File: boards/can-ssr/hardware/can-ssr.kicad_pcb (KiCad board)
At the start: 2 copper layers, 100 x 100 mm, 127 parts, among them J1 CAN IN, J2 CAN OUT, J3 ICSP, J30 MEAN WELL, J4 UART, Q1 IPB110N20N3LF, Q2 IPB110N20N3LF, Q20 2N7002, Q21 2N7002, Q22 2N7002, Q23 2N7002, Q24 2N7002, Q3 IPB110N20N3LF, Q4 IPB110N20N3LF, Q5 MMBT2907A, SW1 ADDR, U1 R-78E5.0-1.0, U10 VOM1271T, U11 VOM1271T, U12 ACS770ECB-100U-PFF-T, U2 MCP2562FD-E/P, U20 LM393B, U3 PIC18F47Q84-I/PT, U30 UCC12050DVE, U31 ISO1640DWR, U32 MCP3426A0-E/SN, U33 MCP4725A0T-E/CH, U34 MCP4725A0T-E/CH, U35 TLP222A, U36 MCP3426A1-E/SN, U40 MAX7219CWG+, U41 CC56-12SRWA, Y1 16MHz

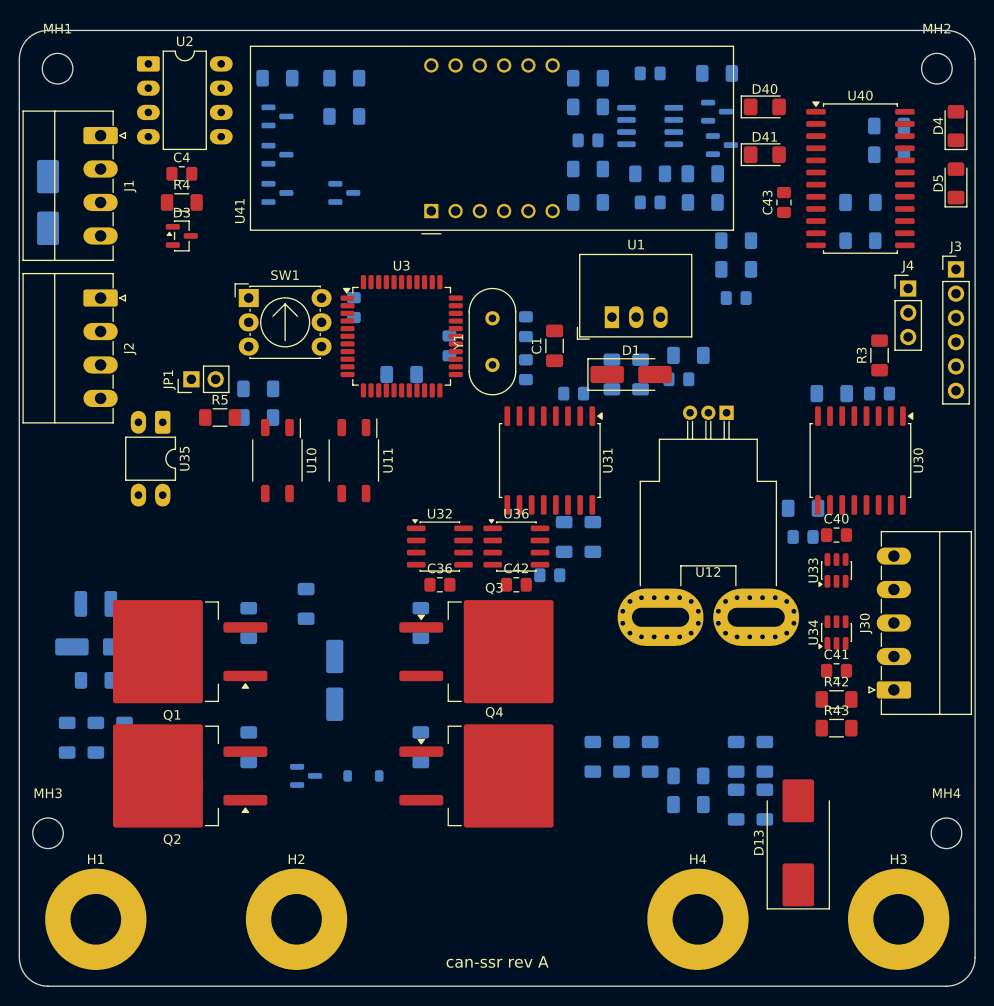
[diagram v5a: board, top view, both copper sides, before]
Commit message: can-ssr: power copper, barrier keep-out, busbar strips, HV rules
- Top pours: VIN, SRC, VOUT_SW, VOUT; RET at the S-/L- bolts; GND_LOAD
  pour across the load half on the bottom; logic GND both sides
- 6 mm barrier keep-out (y 42-48) on both layers
- Solder-mask openings for the bars: VIN, VOUT_SW, VOUT (1/2 in), source
  node (1/4 in), return bar (bottom); 12-via rings at S- and L-
- Net classes HV and GD plus 1.5 mm clearance rules in can-ssr.kicad_dru
- L+ moved to x 86 for a straight VOUT bar; D13, DACs and dividers to
  the bottom; dividers chained end to end; MH3 clear of the S+ bar

Co-Authored-By: Claude Opus 5.5 <noreply@anthropic.com>
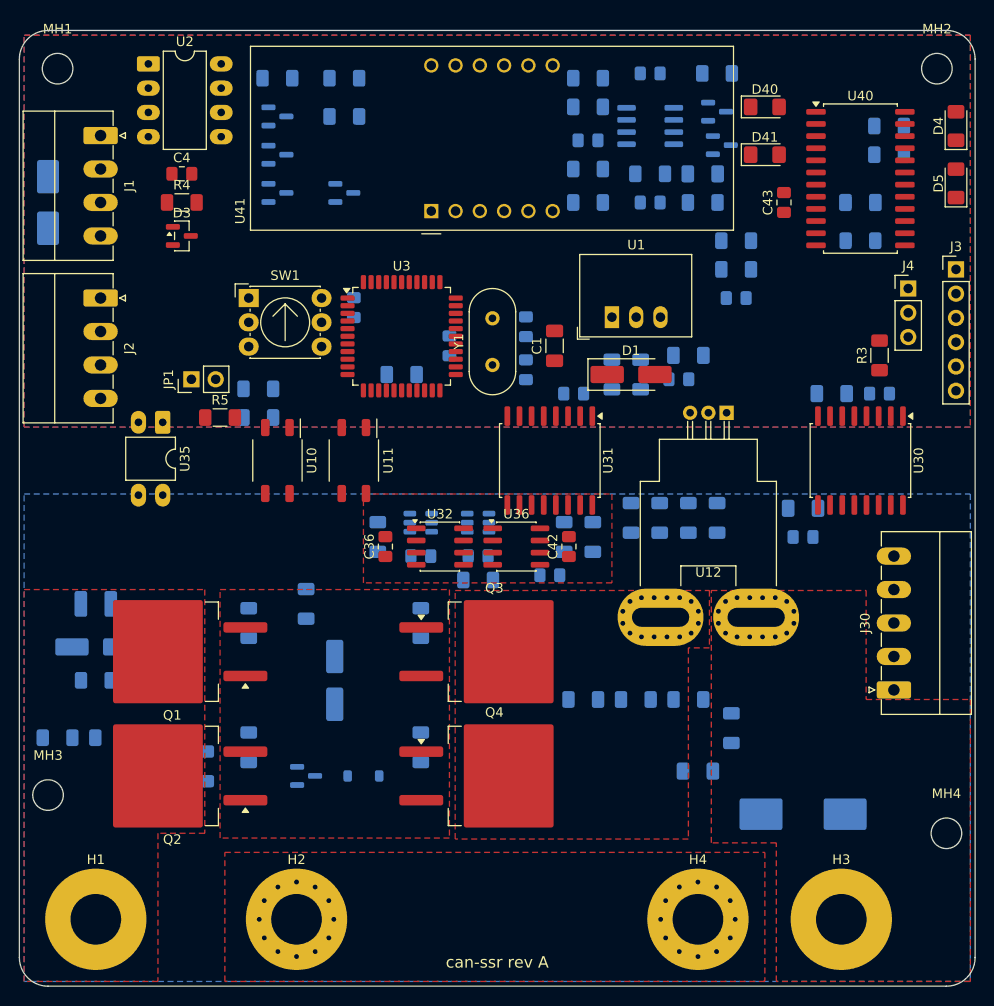
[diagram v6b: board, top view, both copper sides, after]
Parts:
- C40, C41, D13, R42, R43, U33, U34: moved to B.Cu
- moved R42 50.9 mm to (137.5, 153.0), turned to 90 degrees
- moved U33 43.8 mm to (142.0, 151.5), turned to 0 degrees
- moved C40 43.6 mm to (142.0, 155.0)
- moved R43 40.6 mm to (148.0, 157.5)
- moved C41 39.4 mm to (148.0, 155.0)
- moved U34 39.2 mm to (148.0, 151.5), turned to 0 degrees
- moved R45 31.0 mm to (167.0, 151.0)
- moved R47 30.4 mm to (173.0, 151.0)
- moved R44 27.3 mm to (164.0, 151.0)
- moved R46 26.2 mm to (170.0, 151.0)
- moved R40 7.21 mm to (170.0, 170.0), turned to 0 degrees
- moved C36 6.96 mm to (138.3, 154.0), turned to 90 degrees
- moved C42 6.80 mm to (157.5, 154.0), turned to 90 degrees
- moved R41 6.73 mm to (174.5, 173.0), turned to 90 degrees
- moved R39 6.18 mm to (164.5, 170.0), turned to 0 degrees
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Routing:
- net GND_LOAD: vias 0 -> 24
- added copper zone on F.Cu, net /Power path/SRC
- added copper zone on F.Cu, net /Power path/VOUT_SW
- added copper zone on B.Cu, net GND
- added copper zone on F.Cu, net GND
- added copper zone on B.Cu, net GND_LOAD
- added copper zone on F.Cu, net GND_LOAD
- added copper zone on F.Cu, net VIN
- added copper zone on F.Cu, net VOUT

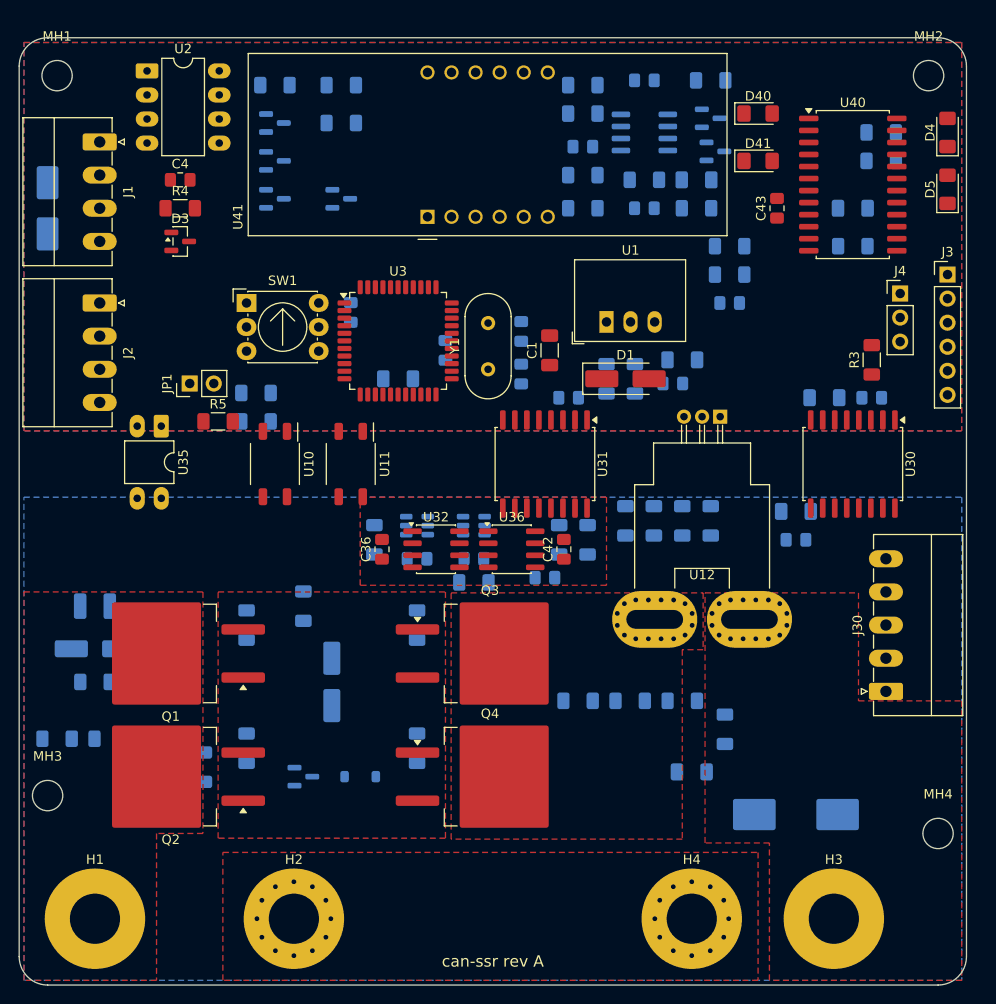
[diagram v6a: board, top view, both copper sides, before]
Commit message: can-ssr: routing (work in progress)
- Routed in passes with Freerouting (headless, via Specctra DSN/SES):
  A) gate-drive and HV nets alone; B) all other nets with A locked and
  1.5 mm clearance around HV/gate-drive copper; keep-outs over the power
  pours, busbars and the return-bar area
- VOM1271s, Q5/D11 moved to the left end of the barrier; Vin divider
  chain moved toward the ADC; TLP222A to the right end of the barrier
  next to J30; divider internal nodes added to the VIN-to-gate rule
- Ground stitching vias at S-/L- and in pour islands; 2 mm V12_BUS
  pass-through between J1 and J2
- No clearance or short violations. Still open: 37 ground-pour island
  connections, DISP_LOAD and SEG_F, starved thermals, silkscreen

Co-Authored-By: Claude Opus 5.5 <noreply@anthropic.com>
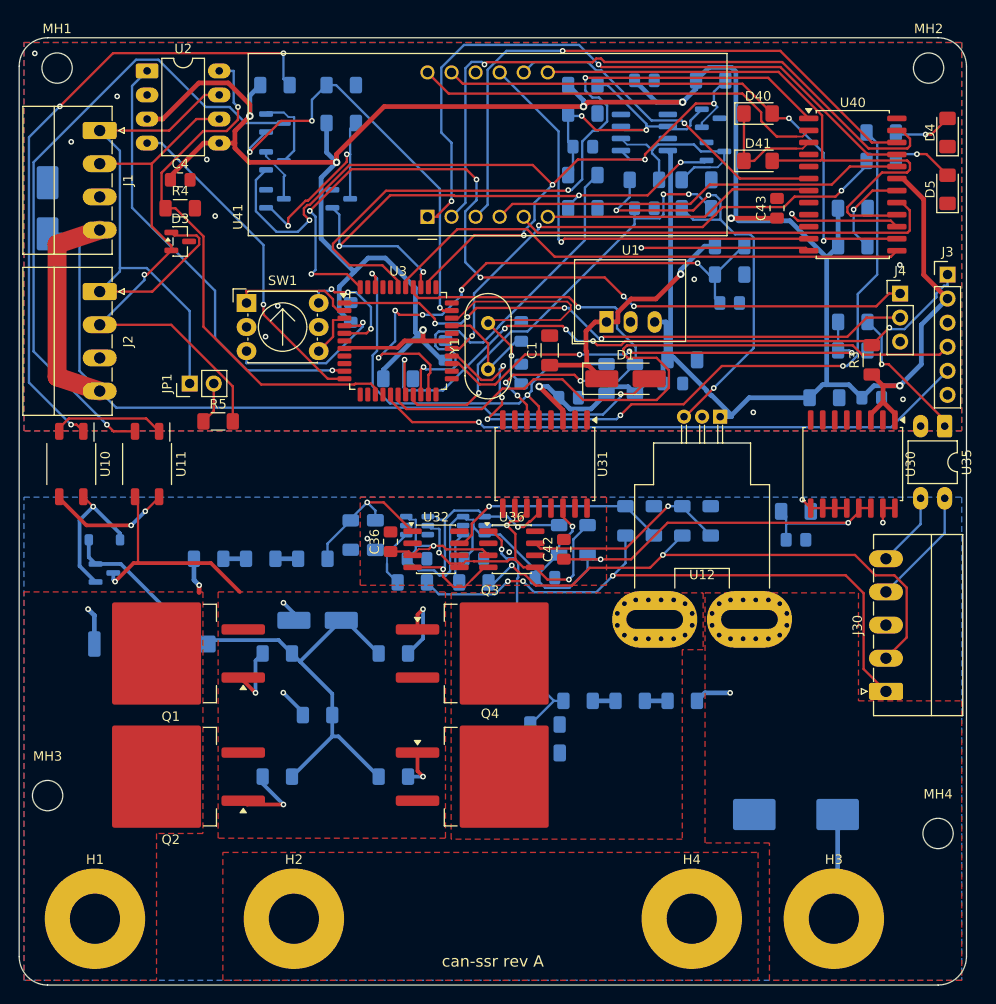
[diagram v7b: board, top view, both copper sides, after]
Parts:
- moved U35 82.7 mm to (197.7, 141.0)
- moved R48 63.4 mm to (188.0, 130.0)
- moved R49 63.4 mm to (188.0, 133.0)
- moved D11 36.8 mm to (109.0, 153.0)
- moved C37 34.1 mm to (137.6, 152.5), turned to -90 degrees
- moved Q5 30.1 mm to (109.0, 156.5)
- moved R37 29.0 mm to (135.0, 152.5), turned to -90 degrees
- moved R34 24.8 mm to (120.0, 155.0)
- moved R35 24.8 mm to (125.5, 155.0)
- moved R36 24.8 mm to (131.0, 155.0)
- moved U10 21.5 mm to (105.5, 145.0)
- moved U11 21.5 mm to (113.5, 145.0)
- moved R41 19.0 mm to (155.5, 172.5), turned to 0 degrees
- moved C38 15.6 mm to (155.5, 175.5)
- moved R14 11.6 mm to (131.5, 171.5), turned to 180 degrees
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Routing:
- net +5V: track 0.00 -> 329.9 mm, vias 0 -> 8
- net /Load-side sense and supply control/V5_ISO: track 0.00 -> 109.8 mm, vias 0 -> 4
- net /CAN, power, MCU/V12_BUS: track 0.00 -> 107.6 mm, vias 0 -> 1
- net TRIP_OK: track 0.00 -> 91.8 mm, vias 0 -> 5
- net /CAN, power, MCU/UART_TX: track 0.00 -> 90.3 mm, vias 0 -> 6
- net /CAN, power, MCU/LED_STATUS: track 0.00 -> 80.5 mm, vias 0 -> 5
- net DISP_DIN: track 0.00 -> 77.4 mm, vias 0 -> 2
- net /CAN, power, MCU/ICSPDAT: track 0.00 -> 75.3 mm
- net /CAN, power, MCU/MCLR: track 0.00 -> 72.4 mm, vias 0 -> 5
- net /Display/SEG_E: track 0.00 -> 71.8 mm, vias 0 -> 2
- net /Display/SEG_D: track 0.00 -> 70.4 mm, vias 0 -> 1
- net VOM_LED_A: track 0.00 -> 67.9 mm, vias 0 -> 3
- net VOM_LED_K: track 0.00 -> 67.8 mm, vias 0 -> 1
- net /CAN, power, MCU/CANH: track 0.00 -> 66.3 mm
- net /Power path/GATE: track 0.00 -> 66.1 mm
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
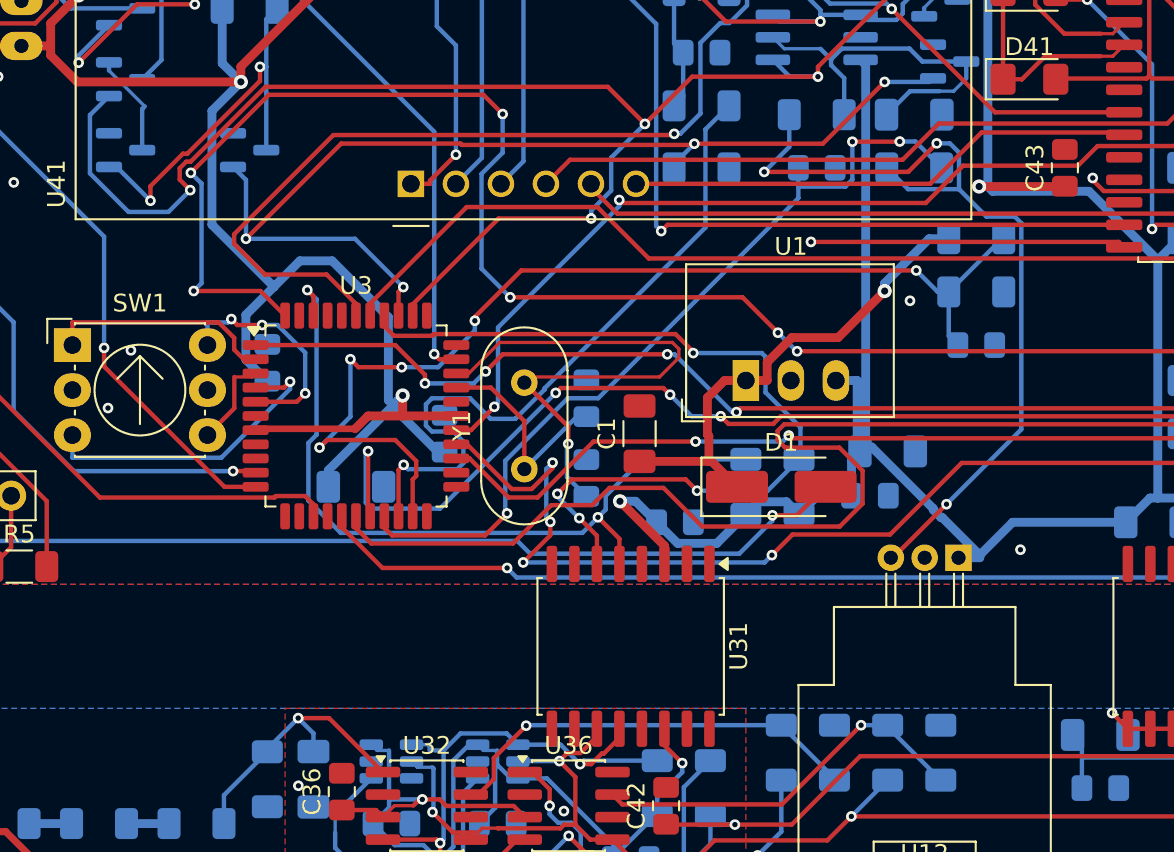
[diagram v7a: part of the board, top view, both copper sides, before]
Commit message: can-ssr: more ground stitching (33 open ground links left)
Co-Authored-By: Claude Opus 5.5 <noreply@anthropic.com>
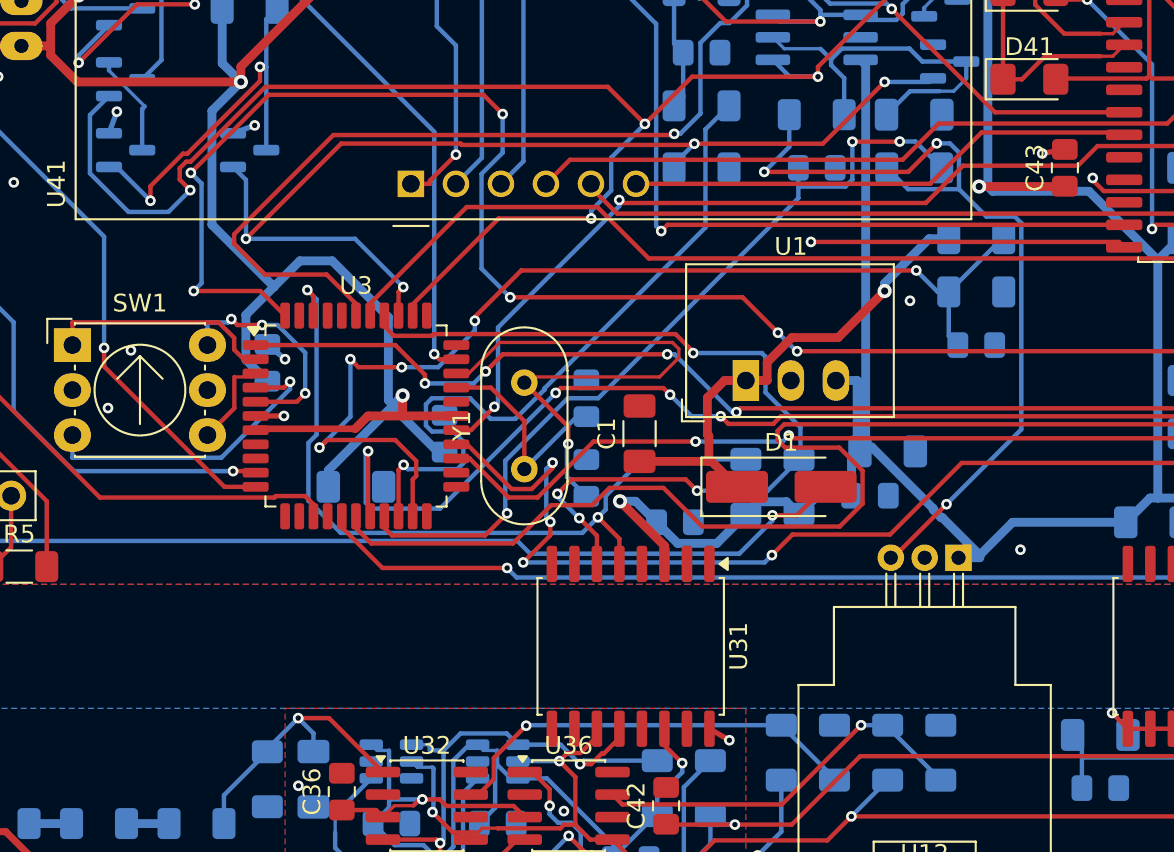
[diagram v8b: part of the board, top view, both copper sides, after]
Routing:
- net GND: track 0.00 -> 6.80 mm, vias 11 -> 16
- net GND_LOAD: track 7.87 -> 9.17 mm, vias 4 -> 5
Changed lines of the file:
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@@
+	)
+	(segment
+		(start 159.945 149.65)
+		(end 161.070833 150.3)
+		(width 0.3)
+		(layer "F.Cu")
+		(net "GND_LOAD")
 	)
 	(segment
@@
 	(via
 		(at 191.175 151.1817)
+		(size 0.6)
+		(drill 0.3)
+		(layers "F.Cu" "B.Cu")
+		(net "GND_LOAD")
+	)
+	(via
+		(at 161.070833 150.3)
 		(size 0.6)
 		(drill 0.3)
@@
 		(net "/CAN, power, MCU/ADDR3")
 	)
+	(segment
+		(start 134.3375 132)
+		(end 135.9375 132)
+		(width 0.3)
+		(layer "F.Cu")
+		(net "GND")
+	)
+	(segment
+		(start 180 116.9625)
+		(end 178.719749 117.188242)
+		(width 0.3)
+		(layer "F.Cu")
+		(net "GND")
+	)
 	(via
 		(at 171.2622 125.501691)
@@
 	)
 	(via
+		(at 134.2841 115.605373)
+		(size 0.6)
+		(drill 0.3)
+		(layers "F.Cu" "B.Cu")
+		(net "GND")
+	)
+	(via
 		(at 177.495 139.546438)
 		(size 0.6)
@@
 	)
 	(via
+		(at 135.9375 132)
+		(size 0.6)
+		(drill 0.3)
+		(layers "F.Cu" "B.Cu")
+		(net "GND")
+	)
+	(via
 		(at 120.6892 118.822634)
 		(size 0.6)
@@
 		(net "GND")
 	)
+	(via
+		(at 178.719749 117.188242)
+		(size 0.6)
+		(drill 0.3)
+		(layers "F.Cu" "B.Cu")
+		(net "GND")
+	)
+	(via
+		(at 135.995857 128.798123)
+		(size 0.6)
+		(drill 0.3)
+		(layers "F.Cu" "B.Cu")
+		(net "GND")
+	)
+	(via
+		(at 126.507126 114.828399)
+		(size 0.6)
+		(drill 0.3)
+		(layers "F.Cu" "B.Cu")
+		(net "GND")
+	)
+	(segment
+		(start 135 127.9625)
+		(end 135.995857 128.798123)
+		(width 0.3)
+		(layer "B.Cu")
+		(net "GND")
+	)
+	(segment
+		(start 133.0625 116.05)
+		(end 134.2841 115.605373)
+		(width 0.3)
+		(layer "B.Cu")
+		(net "GND")
+	)
+	(segment
+		(start 126.0625 116.05)
+		(end 126.507126 114.828399)
+		(width 0.3)
+		(layer "B.Cu")
+		(net "GND")
+	)
